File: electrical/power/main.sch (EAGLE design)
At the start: 0 parts

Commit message: start hot things pcba
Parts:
- added U$1: FUSE_HOLDER_1.25X0.25IN, power_supplies:FUSE_HOLDER_1.25X0.25IN
- added U$2: FUSE_HOLDER_0.205X0.787IN, power_supplies:FUSE_HOLDER_0.205X0.787IN
- added U$3, U$4: DG85BM-5011-76-1024, power_supplies:DG85BM-5011-76-1024
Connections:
- new net 36V: U$1.1, U$2.1
- new net 5V: U$1.5V, U$2.5V
- new net AGND: U$3.P$87A_B, U$3.P$87A_T
- new net N$1: U$1.3, U$3.P$87_B, U$3.P$87_T
- new net N$3: U$2.3, U$4.P$87_B, U$4.P$87_T
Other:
- note added: "CONNECTORS"
- note added: "Connector to Integration PCBA"
- note added: "FUSE INLINE"
- note added: "OUTPUT TO DRIVE POWER SUPPLY"
- note added: "OUTPUT TO MOWER"

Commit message: clean power schematic
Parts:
- removed U$1: FUSE_HOLDER_1.25X0.25IN, power_supplies:FUSE_HOLDER_1.25X0.25IN
- removed U$2: FUSE_HOLDER_0.205X0.787IN, power_supplies:FUSE_HOLDER_0.205X0.787IN
- removed U$3, U$4: DG85BM-5011-76-1024, power_supplies:DG85BM-5011-76-1024
- added FH1: FUSE_HOLDER_1.25X0.25IN, power_supplies:FUSE_HOLDER_1.25X0.25IN
- added FH2: FUSE_HOLDER_0.205X0.787IN, power_supplies:FUSE_HOLDER_0.205X0.787IN
- added U1: VS-STPS20L15DPBF, discrete:VS-STPS20L15DPBF
- added U2, U3: DG85BM-5011-76-1024, power_supplies:DG85BM-5011-76-1024
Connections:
- removed net AGND: U$3.P$87A_B, U$3.P$87A_T
- new net !UVLO!: U1.OUTA
- new net 5V_CPU: U1.VDD2
- new net GND: U1.GND, U1.GND1, U1.GND_2, U1.GND_3, U1.GND_4, U1.INB+, U1.V-, U1.VINN, U2.P$87A_B, U2.P$87A_T
- new net GND_CPU: U1.GND2, U2.C
- new net MOW_EN: U2.E
- new net N$2: U1.VINP, U2.P$86_B', U2.P$86_T
- new net N$4: U1.INA-, U2.A, U2.P$85_B, U2.P$85_T
- new net N$6: U3.P$86_B', U3.P$86_T
- new net N$7: U3.P$85_B, U3.P$85_T
- net 36V: now also FH1.1, FH1.2, FH2.1, FH2.2, U1.IN; no longer U$1.1, U$2.1
- net 5V: now also U1.INB-, U1.OUT, U1.V+, U1.VDD1, U2.CO; no longer U$1.5V, U$2.5V
- net N$1: now also FH1.3, FH1.4, U1.OUTB, U1.VOUTN, U2.P$87_B, U2.P$87_T; no longer U$1.3, U$3.P$87_B, U$3.P$87_T
- net N$3: now also FH2.3, FH2.4, U1.INA+, U1.VOUTP, U3.P$87_B, U3.P$87_T; no longer U$2.3, U$4.P$87_B, U$4.P$87_T
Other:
- note added: "36V to 5V Linear Regulator"
- note added: "CPU/Sensor power supply is derived from battery 36V. If mower noise becomes an issue, will use separate battery system for CPU/sensor. Isolators allow for communication between systems in that event."
- note added: "Drive Motor Relay Coil Control"
- note added: "Isolate Battery Voltage Sense"
- note added: "Isolate Mower Enable"
- note added: "Mow Motor Relay Coil Control"
- note added: "Protect batteries by disabling relays when battery voltage below threshold"
- note added: "Reed Switch to magnetic safety tether"
- note added: "Relay coil drives, enables, and Unver Voltage LockOut"

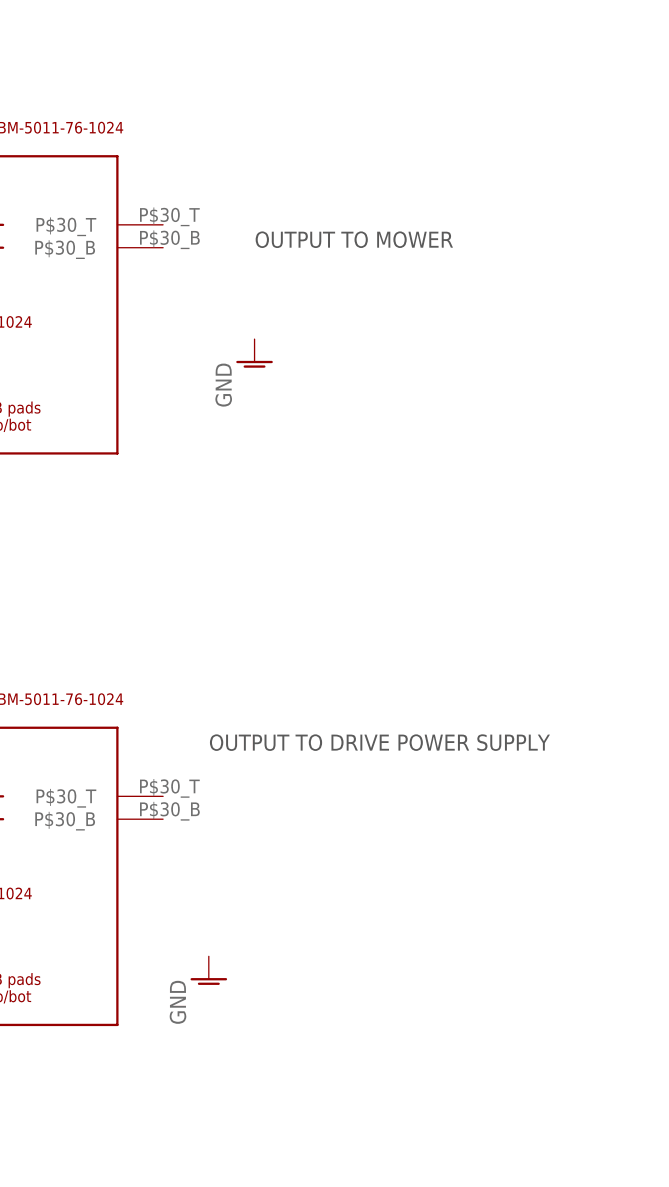
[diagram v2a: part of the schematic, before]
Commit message: add phoenix contact 40A two term modular connector
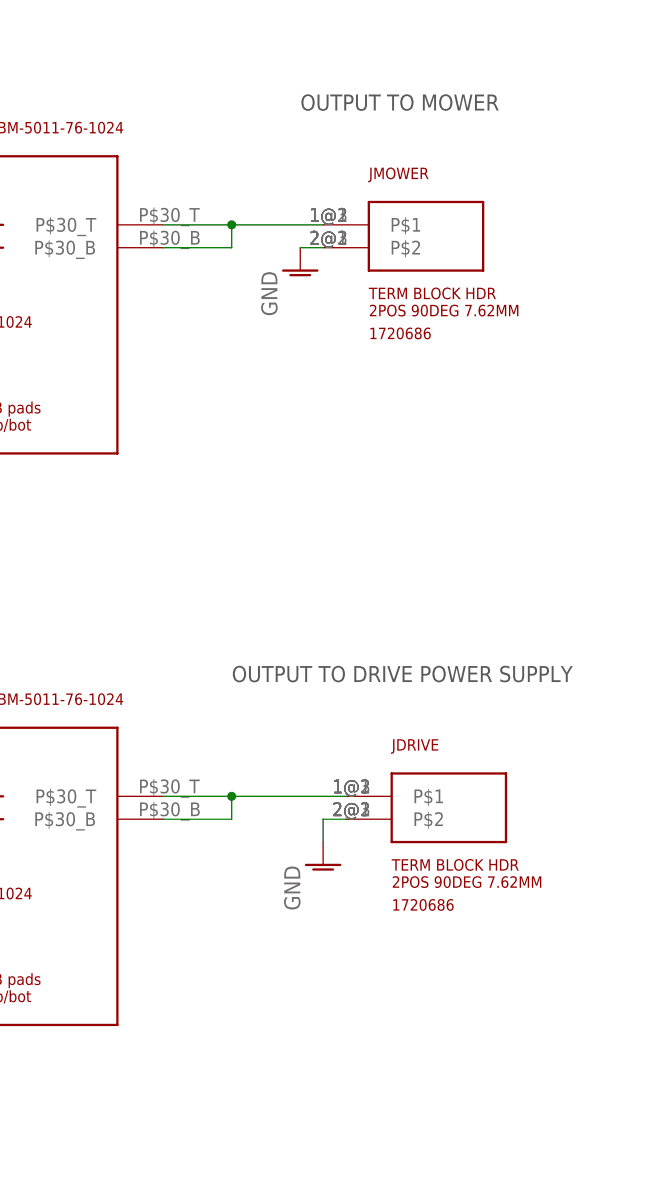
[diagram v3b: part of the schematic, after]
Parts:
- added JDRIVE, JMOWER: 1720686, power_connectors:1720686
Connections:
- new net N$8: JMOWER.P$1@1, U2.P$30_B, U2.P$30_T
- new net N$9: JDRIVE.P$1@1, U3.P$30_B, U3.P$30_T
- net GND: now also JDRIVE.P$2@1, JMOWER.P$2@1
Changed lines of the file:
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@@
 <part name="U$3" library="power_supplies" deviceset="5V" device=""/>
 <part name="GND6" library="power_supplies" deviceset="GND" device=""/>
+<part name="JMOWER" library="power_connectors" deviceset="1720686" device=""/>
+<part name="JDRIVE" library="power_connectors" deviceset="1720686" device=""/>
 </parts>
 <sheets>
@@
 <text x="33.02" y="167.64" size="1.778" layer="97">FUSE INLINE</text>
 <text x="33.02" y="165.1" size="1.778" layer="97">CONNECTORS</text>
-<text x="213.36" y="144.78" size="1.778" layer="97">OUTPUT TO MOWER</text>
-<text x="208.28" y="88.9" size="1.778" layer="97">OUTPUT TO DRIVE POWER SUPPLY</text>
+<text x="218.44" y="160.02" size="1.778" layer="97">OUTPUT TO MOWER</text>
+<text x="210.82" y="96.52" size="1.778" layer="97">OUTPUT TO DRIVE POWER SUPPLY</text>
 </plain>
 <moduleinsts>
@@
 <instance part="36V1" gate="A" x="50.8" y="147.32"/>
 <instance part="36V3" gate="A" x="91.44" y="86.36"/>
-<instance part="GND3" gate="VR1" x="213.36" y="132.08"/>
-<instance part="GND2" gate="VR1" x="208.28" y="63.5"/>
+<instance part="GND3" gate="VR1" x="218.44" y="142.24"/>
+<instance part="GND2" gate="VR1" x="220.98" y="76.2"/>
 <instance part="U1" gate="A" x="121.92" y="20.32"/>
 <instance part="36V2" gate="A" x="86.36" y="149.86"/>
@@
 <instance part="U$3" gate="A" x="12.7" y="147.32"/>
 <instance part="GND6" gate="VR1" x="15.24" y="109.22"/>
+<instance part="JMOWER" gate="G$1" x="220.98" y="147.32"/>
+<instance part="JDRIVE" gate="G$1" x="223.52" y="83.82"/>
 </instances>
 <busses>
@@
 <wire x1="33.02" y1="15.24" x2="33.02" y2="17.78" width="0.1524" layer="91"/>
 </segment>
+<segment>
+<pinref part="JMOWER" gate="G$1" pin="P$2@1"/>
+<pinref part="GND3" gate="VR1" pin="GND"/>
+<wire x1="218.44" y1="144.78" x2="220.98" y2="144.78" width="0.1524" layer="91"/>
+</segment>
+<segment>
+<pinref part="GND2" gate="VR1" pin="GND"/>
+<wire x1="220.98" y1="78.74" x2="220.98" y2="81.28" width="0.1524" layer="91"/>
+<pinref part="JDRIVE" gate="G$1" pin="P$2@1"/>
+<wire x1="220.98" y1="81.28" x2="223.52" y2="81.28" width="0.1524" layer="91"/>
+</segment>
 </net>
 <net name="5V" class="0">
@@
 </segment>
 </net>
+<net name="N$8" class="0">
+<segment>
+<pinref part="U2" gate="G$1" pin="P$30_B"/>
+<wire x1="203.2" y1="144.78" x2="210.82" y2="144.78" width="0.1524" layer="91"/>
+<wire x1="210.82" y1="144.78" x2="210.82" y2="147.32" width="0.1524" layer="91"/>
+<pinref part="JMOWER" gate="G$1" pin="P$1@1"/>
+<wire x1="210.82" y1="147.32" x2="220.98" y2="147.32" width="0.1524" layer="91"/>
+<pinref part="U2" gate="G$1" pin="P$30_T"/>
+<wire x1="210.82" y1="147.32" x2="203.2" y2="147.32" width="0.1524" layer="91"/>
+<junction x="210.82" y="147.32"/>
+</segment>
+</net>
+<net name="N$9" class="0">
+<segment>
+<pinref part="U3" gate="G$1" pin="P$30_B"/>
+<wire x1="203.2" y1="81.28" x2="210.82" y2="81.28" width="0.1524" layer="91"/>
+<wire x1="210.82" y1="81.28" x2="210.82" y2="83.82" width="0.1524" layer="91"/>
+<pinref part="JDRIVE" gate="G$1" pin="P$1@1"/>
+<wire x1="210.82" y1="83.82" x2="223.52" y2="83.82" width="0.1524" layer="91"/>
+<pinref part="U3" gate="G$1" pin="P$30_T"/>
+<wire x1="203.2" y1="83.82" x2="210.82" y2="83.82" width="0.1524" layer="91"/>
+<junction x="210.82" y="83.82"/>
+</segment>
+</net>

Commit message: make stupid diode symbol look like a diode. add power connectors to sch
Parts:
- removed U1: VS-STPS20L15DPBF, discrete:VS-STPS20L15DPBF
- added D1: VS-STPS20L15DPBF, discrete:VS-STPS20L15DPBF
- added J_CPU: 1720686, power_connectors:1720686
- added U$4: 1996236, power_connectors:1996236
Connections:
- removed net !UVLO!: U1.OUTA
- removed net 5V_CPU: U1.VDD2
- new net N$10: D1.1, D1.2, J_CPU.P$2@1, J_CPU.P$2@2, J_CPU.P$2@3
- net 36V: now also D1.3, U$4.P$2@1, U$4.P$2@2, U$4.P$2@3; no longer U1.IN
- net 5V: now also U$4.5V; no longer U1.INB-, U1.OUT, U1.V+, U1.VDD1
- net GND: now also JDRIVE.P$1@1, JMOWER.P$1@1, J_CPU.P$1@1, J_CPU.P$1@2, J_CPU.P$1@3, U$4.P$1@1, U$4.P$1@2, U$4.P$1@3; no longer JDRIVE.P$2@1, JMOWER.P$2@1, U1.GND, U1.GND1, U1.GND_2, U1.GND_3, U1.GND_4, U1.INB+, U1.V-, U1.VINN
- net GND_CPU: no longer U1.GND2
- net N$1: no longer U1.OUTB, U1.VOUTN
- net N$2: no longer U1.VINP
- net N$3: no longer U1.INA+, U1.VOUTP
- net N$4: no longer U1.INA-
- net N$8: now also JMOWER.P$2@1; no longer JMOWER.P$1@1
- net N$9: now also JDRIVE.P$2@1; no longer JDRIVE.P$1@1
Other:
- note added: "Battery Input"
- note added: "Fuse inline on cable 50A"
- note added: "To CPU/Sensor"
- note removed: "CONNECTORS"
- note removed: "FUSE INLINE"
- moved on the sheet: JDRIVE, JMOWER

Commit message: add power diode. move relays off board
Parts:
- removed D1: VS-STPS20L15DPBF, discrete:VS-STPS20L15DPBF
- removed U2, U3: DG85BM-5011-76-1024, power_supplies:DG85BM-5011-76-1024
- added D2: STPS20M60D, discrete:STPS20M60D
- added FH3: FUSE_HOLDER_0.205X0.787IN, power_supplies:FUSE_HOLDER_0.205X0.787IN
- added JDRV_CL, JMOW_CL: 1720686, power_connectors:1720686
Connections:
- removed net GND_CPU: U2.C
- removed net MOW_EN: U2.E
- new net N$11: D2.3, FH3.3, FH3.4
- net 36V: now also FH3.1, FH3.2; no longer D1.3
- net 5V: no longer U2.CO
- net GND: now also JDRIVE.P$1@2, JDRIVE.P$1@3, JMOWER.P$1@2, JMOWER.P$1@3; no longer U2.P$87A_B, U2.P$87A_T
- net N$1: no longer U2.P$87_B, U2.P$87_T
- net N$10: now also D2.1, D2.2; no longer D1.1, D1.2
- net N$2: now also JMOW_CL.P$2@1; no longer U2.P$86_B', U2.P$86_T
- net N$3: no longer U3.P$87_B, U3.P$87_T
- net N$4: now also JMOW_CL.P$1@1; no longer U2.A, U2.P$85_B, U2.P$85_T
- net N$6: now also JDRV_CL.P$2@1; no longer U3.P$86_B', U3.P$86_T
- net N$7: now also JDRV_CL.P$1@1, JDRV_CL.P$1@2, JDRV_CL.P$1@3; no longer U3.P$85_B, U3.P$85_T
- net N$8: now also JMOWER.P$2@2, JMOWER.P$2@3; no longer U2.P$30_B, U2.P$30_T
- net N$9: now also JDRIVE.P$2@2, JDRIVE.P$2@3; no longer U3.P$30_B, U3.P$30_T
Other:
- note added: "2.5V biased differential out Use single ended"
- note added: "Battery In 30-42V in 36V nominal 50A max, Fuse inline on cable"
- note added: "Max supply current dominated by analog isolator: 6mA in our operating conditions Max power at full bat: 0.252W"
- note added: "OUTPUT TO DRIVE MOTOR POWER SUPPLY RELAY 16A Max RELAY PN: PRD-5DY0-24 50V DC / 25A Coil :24V @ 2W"
- note added: "OUTPUT TO MOWER RELAY 25A max stall RELAY PN: PRD-5DY0-24 50V DC / 25A Coil :24V @ 2W"
- note added: "To CPU/Sensor 1.3A nominal 5A MAX burst for deck adjust actuators"
- note added: "map 42V max bat to 250mV in"
- note added: "todo: set threshold resistors"
- note added: "todo: size/spec resistors for constant current have to be kinda big"
- note removed: "Fuse inline on cable 50A"
- note removed: "OUTPUT TO DRIVE POWER SUPPLY"
- note removed: "OUTPUT TO MOWER"
- note removed: "To CPU/Sensor"
- moved on the sheet: FH1, FH2, JDRIVE, JMOWER, J_CPU

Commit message: spec power for coil drive components. spec uvlo hysteresis.
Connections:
- removed net 5V: U$4.5V
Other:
- note added: "260 to 317 ohm coil resistance 24V to drive coil Set I = 83mA RCCM = RCCD = 4.3/0.083 ~= 52R PWR = 0.083^2 * 52 = 0.358W At max vbat 42V and lowest batch relay coil resistance 260R, CC XSTR drops 11.8V => 1W Need 50x50mm 1oz copper for 1.6W rating"
- note added: "Mower enable toggle"
- note added: "Threshold low: ~30V Threshold high: ~36V"
- note added: "Wires to E-Stop"
- note removed: "todo: set threshold resistors"
- note removed: "todo: size/spec resistors for constant current have to be kinda big"

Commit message: update frame titles stupid eagle
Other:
- note added: "1/5"
- note added: "2/5"
- note added: "3/5"
- note added: "4/5"
- note added: "5/5"
- note added: "5V REGULATOR"
- note added: "CPU_ISOLATION"
- note added: "RELAY COIL DRIVE"
- note added: "Under Voltage Lockout"
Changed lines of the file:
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@@
 <text x="167.64" y="144.78" size="1.778" layer="97" rot="R180">2.5V biased differential out
 Use single ended</text>
+<text x="218.44" y="15.24" size="1.778" layer="94">CPU_ISOLATION</text>
+<text x="228.6" y="5.08" size="1.778" layer="94">2/5</text>
 </plain>
 <instances>
-<instance part="FRAME1" gate="G$1" x="0" y="0"/>
+<instance part="FRAME1" gate="G$1" x="0" y="0" smashed="yes">
+<attribute name="LAST_DATE_TIME" x="217.17" y="10.16" size="2.286" layer="94"/>
+</instance>
 <instance part="U1" gate="A" x="78.74" y="119.38"/>
 <instance part="U2" gate="G$1" x="109.22" y="53.34" rot="MR0"/>
@@
 analog isolator: 6mA in our operating conditions
 Max power at full bat: 0.252W</text>
+<text x="218.44" y="15.24" size="1.778" layer="94">5V REGULATOR</text>
+<text x="231.14" y="5.08" size="1.778" layer="94">3/5</text>
 </plain>
 <instances>
-<instance part="FRAME1" gate="G$1" x="0" y="0"/>
+<instance part="FRAME1" gate="G$1" x="0" y="0" smashed="yes">
+<attribute name="LAST_DATE_TIME" x="217.17" y="10.16" size="2.286" layer="94"/>
+</instance>
 <instance part="U1" gate="A" x="157.48" y="114.3" rot="MR0"/>
 <instance part="U$1" gate="A" x="91.44" y="116.84"/>
@@
 <text x="22.86" y="86.36" size="2.54" layer="97">Threshold low: ~30V
 Threshold high: ~36V</text>
+<text x="218.44" y="15.24" size="1.778" layer="94">Under Voltage Lockout</text>
+<text x="228.6" y="5.08" size="1.778" layer="94">4/5</text>
 </plain>
 <instances>
-<instance part="FRAME1" gate="G$1" x="0" y="0"/>
+<instance part="FRAME1" gate="G$1" x="0" y="0" smashed="yes">
+<attribute name="LAST_DATE_TIME" x="217.17" y="10.16" size="2.286" layer="94"/>
+</instance>
 <instance part="U1" gate="A" x="144.78" y="93.98">
 <attribute name="DESCRIPTION" x="111.76" y="66.04" size="1.778" layer="96"/>
@@
 <text x="134.62" y="137.16" size="2.54" layer="97">Wires to E-Stop</text>
 <text x="165.1" y="124.46" size="2.54" layer="97">Mower enable toggle</text>
+<text x="218.44" y="15.24" size="1.778" layer="94">RELAY COIL DRIVE</text>
+<text x="231.14" y="5.08" size="1.778" layer="94">5/5</text>
 </plain>
 <moduleinsts>
@@
 </moduleinsts>
 <instances>
-<instance part="FRAME1" gate="G$1" x="0" y="0"/>
+<instance part="FRAME1" gate="G$1" x="0" y="0" smashed="yes">
+<attribute name="LAST_DATE_TIME" x="217.17" y="10.16" size="2.286" layer="94"/>
+</instance>
 <instance part="U$1" gate="G$1" x="124.46" y="154.94"/>
 <instance part="U$2" gate="G$1" x="200.66" y="53.34" smashed="yes">
@@
 50A max, Fuse
 inline on cable</text>
+<text x="228.6" y="5.08" size="1.778" layer="94">1/5</text>
 </plain>
 <moduleinsts>
@@
 </moduleinsts>
 <instances>
-<instance part="FRAME1" gate="G$1" x="0" y="0"/>
+<instance part="FRAME1" gate="G$1" x="0" y="0" smashed="yes">
+<attribute name="DRAWING_NAME" x="217.17" y="15.24" size="2.54" layer="94"/>
+<attribute name="LAST_DATE_TIME" x="217.17" y="10.16" size="2.286" layer="94"/>
+</instance>
 <instance part="FH1" gate="A" x="132.08" y="139.7"/>
 <instance part="FH2" gate="A" x="121.92" y="68.58"/>

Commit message: clean some DRC
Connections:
- removed net N$1: FH1.3, FH1.4
- removed net N$3: FH2.3, FH2.4
- net N$8: now also FH1.3, FH1.4
- net N$9: now also FH2.3, FH2.4
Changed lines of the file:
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@@
 <setting verticaltext="up"/>
 </settings>
-<grid distance="0.1" unitdist="inch" unit="inch" style="lines" multiple="1" display="no" altdistance="0.05" altunitdist="inch" altunit="inch"/>
+<grid distance="0.1" unitdist="inch" unit="inch" style="lines" multiple="1" display="no" altdistance="0.01" altunitdist="inch" altunit="inch"/>
 <layers>
 <layer number="1" name="Top" color="4" fill="1" visible="no" active="no"/>
@@
 </segment>
 </net>
-<net name="N$1" class="0">
-<segment>
-<wire x1="142.24" y1="139.7" x2="160.02" y2="139.7" width="0.1524" layer="91"/>
-<pinref part="FH1" gate="A" pin="3"/>
-<pinref part="FH1" gate="A" pin="4"/>
-<junction x="142.24" y="139.7"/>
-</segment>
-</net>
-<net name="N$3" class="0">
-<segment>
-<wire x1="147.32" y1="68.58" x2="132.08" y2="68.58" width="0.1524" layer="91"/>
-<pinref part="FH2" gate="A" pin="3"/>
-<pinref part="FH2" gate="A" pin="4"/>
-<junction x="132.08" y="68.58"/>
-</segment>
-</net>
 <net name="N$2" class="0">
 <segment>
@@
 <segment>
 <pinref part="JMOWER" gate="G$1" pin="P$2@1"/>
-<wire x1="167.64" y1="139.7" x2="160.02" y2="139.7" width="0.1524" layer="91"/>
 <pinref part="JMOWER" gate="G$1" pin="P$2@2"/>
+<pinref part="JMOWER" gate="G$1" pin="P$2@3"/>
+<wire x1="142.24" y1="139.7" x2="167.64" y2="139.7" width="0.1524" layer="91"/>
+<pinref part="FH1" gate="A" pin="3"/>
+<pinref part="FH1" gate="A" pin="4"/>
+<junction x="142.24" y="139.7"/>
 <junction x="167.64" y="139.7"/>
-<pinref part="JMOWER" gate="G$1" pin="P$2@3"/>
 </segment>
 </net>
@@
 <segment>
 <pinref part="JDRIVE" gate="G$1" pin="P$2@1"/>
-<wire x1="147.32" y1="68.58" x2="167.64" y2="68.58" width="0.1524" layer="91"/>
 <pinref part="JDRIVE" gate="G$1" pin="P$2@2"/>
+<pinref part="JDRIVE" gate="G$1" pin="P$2@3"/>
+<pinref part="FH2" gate="A" pin="3"/>
+<pinref part="FH2" gate="A" pin="4"/>
+<junction x="132.08" y="68.58"/>
+<wire x1="167.64" y1="68.58" x2="132.08" y2="68.58" width="0.1524" layer="91"/>
 <junction x="167.64" y="68.58"/>
-<pinref part="JDRIVE" gate="G$1" pin="P$2@3"/>
-</segment>
-</net>
+</segment>
+</net>
